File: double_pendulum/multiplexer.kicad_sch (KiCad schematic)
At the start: 12 parts, among them U8 TMUX4051PWR

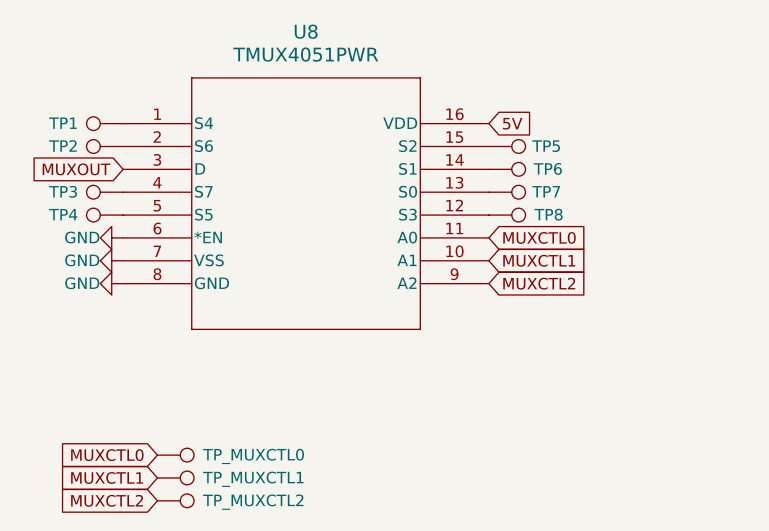
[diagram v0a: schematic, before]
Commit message: Finished schematic and layout of the double pendulum
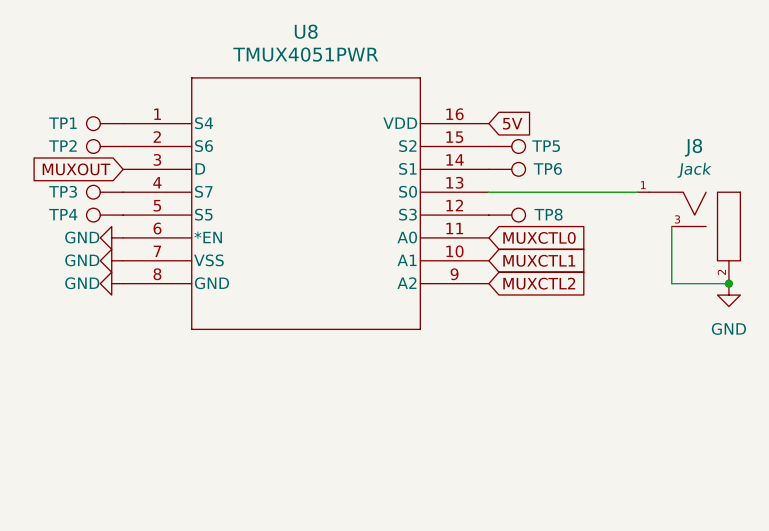
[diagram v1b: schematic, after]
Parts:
- removed TP7, TP_MUXCTL0, TP_MUXCTL1, TP_MUXCTL2: TestPoint, TestPoint:TestPoint_Keystone_5005-5009_Compact, symbol Connector:TestPoint
- added J8: 3.5mm_Mono_Switched_sm, 4ms_Jack:EighthInch_PJ398SM, symbol 4ms_Jack:3.5mm_Mono_Switched_sm
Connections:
- net GND: now also J8.2 (SHEILD), J8.3 (SW)
- net at U8.13 (S0): now also J8.1 (SIG)
